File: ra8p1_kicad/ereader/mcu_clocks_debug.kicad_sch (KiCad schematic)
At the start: 20 parts, among them U1 R7KA8P1KFLCAC#UC0

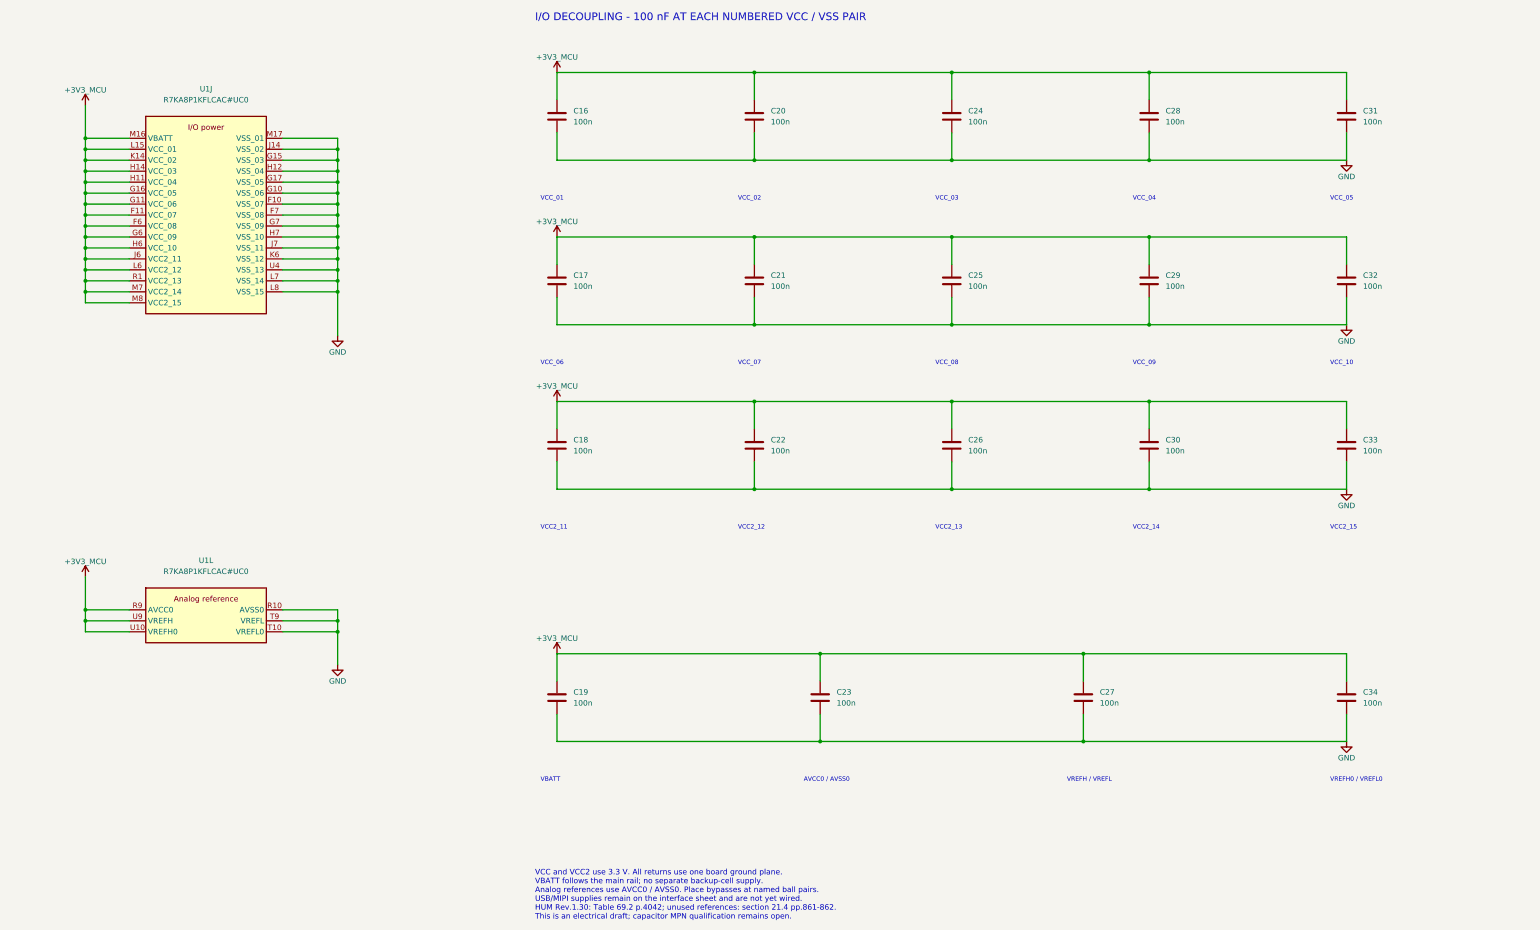
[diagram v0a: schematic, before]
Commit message: feat(hardware): add RA8P1 boot debug draft and refine schematic presentation
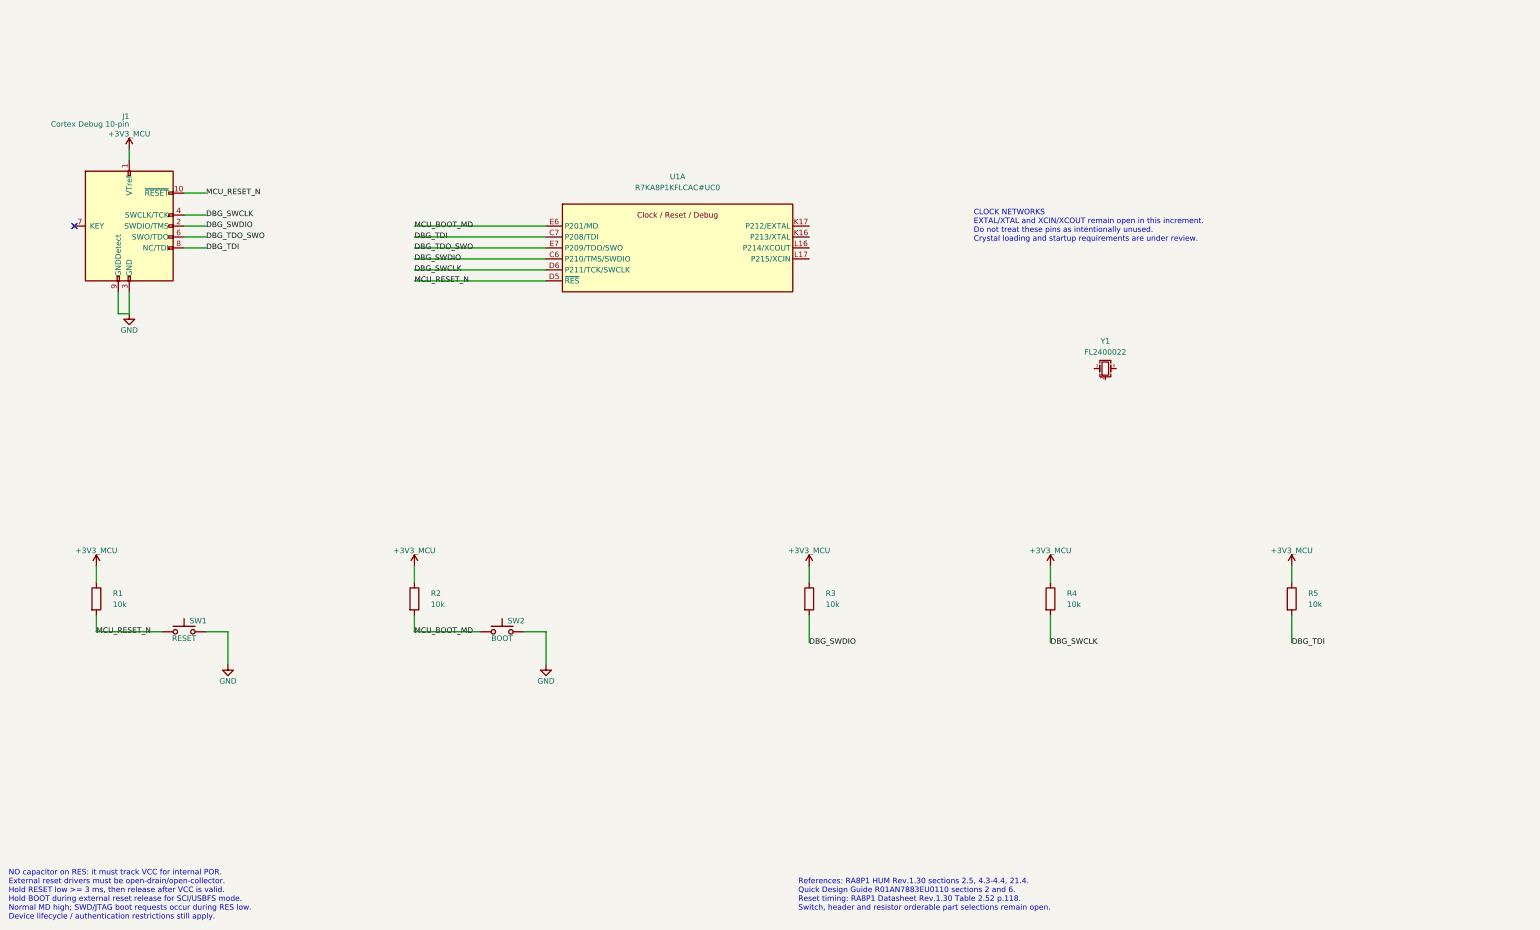
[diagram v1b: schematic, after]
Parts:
- removed C16, C17, C18, C19, C20, C21, C22, C23, C24, C25, C26, C27, C28, C29, C30, C31, C32, C33, C34: 100n, symbol Device:C
- removed U1: R7KA8P1KFLCAC#UC0, Processors:BGA289C65P17X17_1200X1200X138, symbol Processors:R7KA8P1KFLCAC#UC0
- added J1: Cortex Debug 10-pin, symbol Connectors:Cortex_Debug_10_Key
- added R1, R2, R3, R4, R5: 10k, symbol Device:R
- added SW1: RESET, symbol Switch:SW_Push
- added SW2: BOOT, symbol Switch:SW_Push
- added U1: R7KA8P1KFLCAC#UC0, Processors:BGA289C65P17X17_1200X1200X138, symbol Processors:R7KA8P1KFLCAC#UC0
- added Y1: FL2400022, Timing:FL2400022, symbol Device:Crystal_GND24_Small
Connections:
- net +3V3_MCU: now also J1.1 (VTref), R1.1, R2.1, R3.1, R4.1, R5.1
- net GND: now also J1.3 (GND), J1.5 (GND), J1.9 (GNDDetect), SW1.2, SW2.2
- new net: Y1.2 (G), Y1.4 (G)
- new net DBG_SWCLK: J1.4 (SWCLK/TCK), R4.2, U1.D6 (P211/TCK/SWCLK)
- new net DBG_SWDIO: J1.2 (SWDIO/TMS), R3.2, U1.C6 (P210/TMS/SWDIO)
- new net DBG_TDI: J1.8 (NC/TDI), R5.2, U1.C7 (P208/TDI)
- new net DBG_TDO_SWO: J1.6 (SWO/TDO), U1.E7 (P209/TDO/SWO)
- new net MCU_BOOT_MD: R2.2, SW2.1, U1.E6 (P201/MD)
- new net MCU_RESET_N: J1.10 (~{RESET}), R1.2, SW1.1, U1.D5 (~{RES})
- no-connect marks 0 -> 1
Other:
- note added: "CLOCK NETWORKS EXTAL/XTAL and XCIN/XCOUT remain open in this increment. Do not treat these pins as intentionally unused. Crystal loading and startup requirements are under review."
- note added: "NO capacitor on RES: it must track VCC for internal POR. External reset drivers must be open-drain/open-collector. Hold RESET low >= 3 ms, then release after VCC is valid. Hold BOOT during external reset release for SCI/USBFS mode. Normal MD high; SWD/JTAG boot requests occur during RES low. Device lifecycle / authentication restrictions still apply."
- note added: "References: RA8P1 HUM Rev.1.30 sections 2.5, 4.3-4.4, 21.4. Quick Design Guide R01AN7883EU0110 sections 2 and 6. Reset timing: RA8P1 Datasheet Rev.1.30 Table 2.52 p.118. Switch, header and resistor orderable part selections remain open."
- note removed: "AVCC0 / AVSS0"
- note removed: "I/O DECOUPLING - 100 nF AT EACH NUMBERED VCC / VSS PAIR"
- note removed: "VBATT"
- note removed: "VCC and VCC2 use 3.3 V. All returns use one board ground plane. VBATT follows the main rail; no separate backup-cell supply. Analog references use AVCC0 / AVSS0. Place bypasses at named ball pairs. USB/MIPI supplies remain on the interface sheet and are not yet wired. HUM Rev.1.30: Table 69.2 p.4042; unused references: section 21.4 pp.861-862. This is an electrical draft; capacitor MPN qualificat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"
- note removed: "VCC2_11"
- note removed: "VCC2_12"
- note removed: "VCC2_13"
- note removed: "VCC2_14"
- note removed: "VCC2_15"
- note removed: "VCC_01"
- note removed: "VCC_02"
- note removed: "VCC_03"
- note removed: "VCC_04"
- note removed: "VCC_05"
- note removed: "VCC_06"
- note removed: "VCC_07"
- note removed: "VCC_08"
- note removed: "VCC_09"
- note removed: "VCC_10"
- note removed: "VREFH / VREFL"
- note removed: "VREFH0 / VREFL0"
- company: RA8P1 e-reader -> (none)
- title: RA8P1 I/O and analog supplies -> RA8P1 clocks, reset and debug

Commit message: feat(hardware): track schematic BOM and DigiKey sourcing risks
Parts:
- J1: Procurement_Status (none) -> TBD - qualify keyed Cortex 10-pin connector and exact MPN
- R1, R2, R3, R4, R5: Procurement_Status (none) -> TBD - source common 10k 1% resistor with suitable ratings
- SW1, SW2: Procurement_Status (none) -> TBD - source normally-open momentary switch; mechanical cho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
- U1: DigiKey_Part_Number (none) -> 559-R7KA8P1KFLCAC#UC0-ND; DigiKey_URL (none) -> https://www.digikey.com/en/products/detail/renesas-electron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; Procurement_Status (none) -> HOLD - DigiKey discontinued; qualify orderable RA8P1 suffix; Sourcing_Snapshot (none) -> 2026-09-05 indexed: stock 1; USD 29.47; no backorders. Dist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
- Y1: Procurement_Status (none) -> HOLD - oscillator matching and exact MPN sourcing pending
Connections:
- net GND: now also Y1.2 (G), Y1.4 (G)

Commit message: feat(hardware): add Mouser sourcing and qualify MCU pull-up resistors
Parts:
- R1, R2, R3, R4, R5: DigiKey_Part_Number (none) -> 311-10.0KHRCT-ND; DigiKey_URL (none) -> https://www.digikey.com/en/products/detail/yageo/RC0603FR-0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; Manufacturer_Name (none) -> YAGEO; Manufacturer_Part_Number (none) -> RC0603FR-0710KL; Procurement_Status TBD - source common 10k 1% resistor with suitable ratings -> Selected - electrical ratings and sourcing checked; footpri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; Selection_Basis (none) -> 10k 1%, 100mW at 70C, 0603; 3.6V/9.9k=0.364mA and 1.31mW wo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; Sourcing_Snapshot (none) -> 2026-09-05 indexed: stock 2922248; Active; USD CT 1:0.10 / 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
- U1: Mouser Part Number (none) -> 968-R7KA8P1KFLCACUC0; Mouser Price/Stock (none) -> 2026-09-05 browser: 317 in stock; USD 1:29.47 / 10:23.82 / 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; Mouser_URL (none) -> https://www.mouser.com/en/ProductDetail/Renesas-Electronics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; Procurement_Status HOLD - DigiKey discontinued; qualify orderable RA8P1 suffix -> Retain exact UC0 - Mouser stock verified; circuit qualifica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

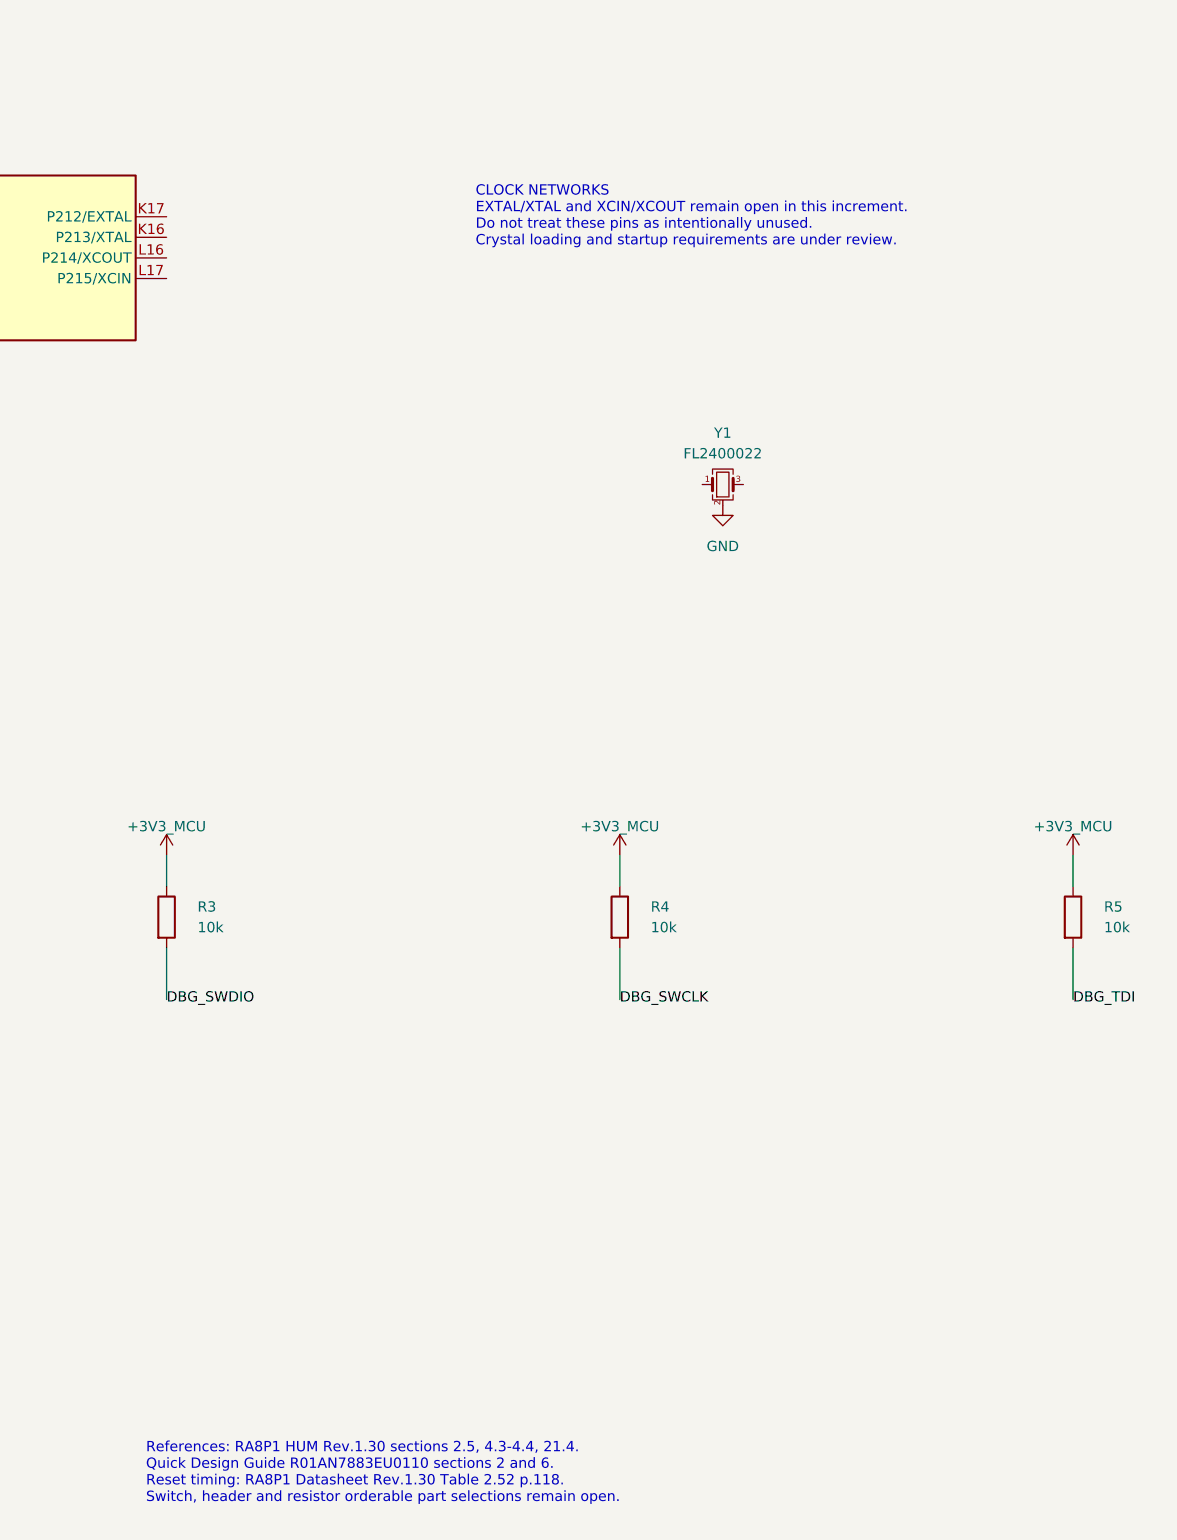
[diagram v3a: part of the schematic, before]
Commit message: feat(hardware): wire main oscillator with traceable load calculations
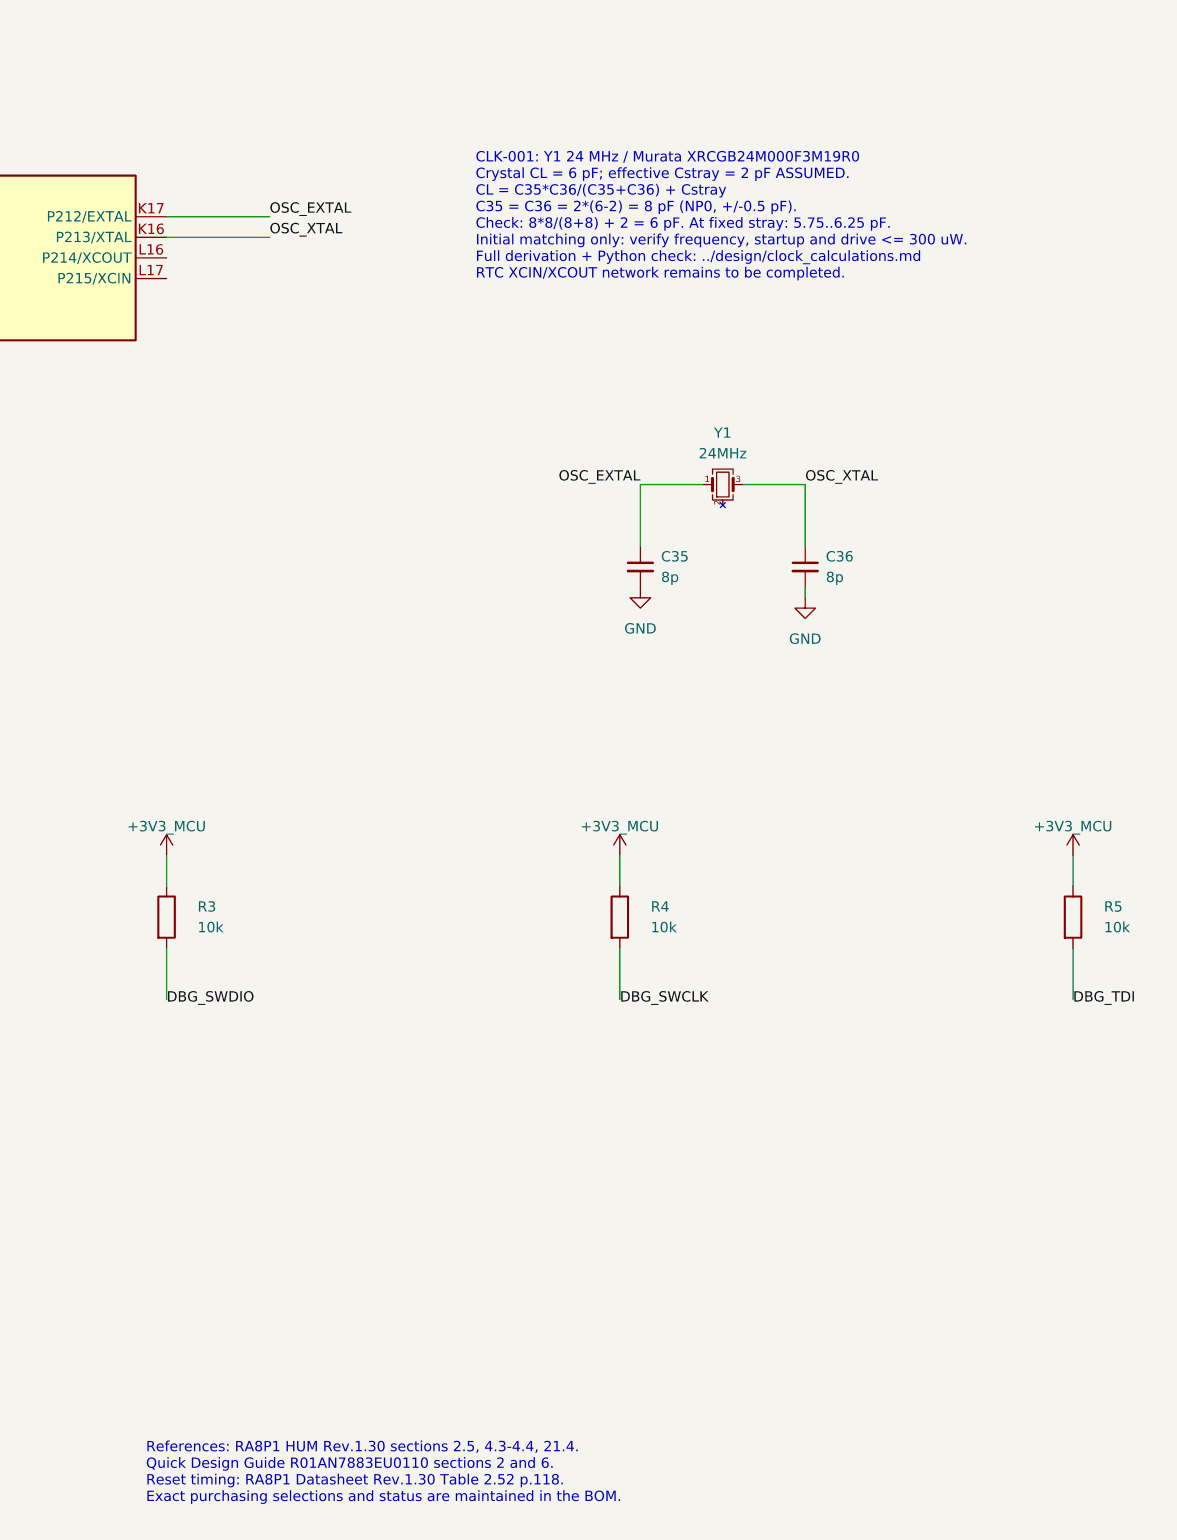
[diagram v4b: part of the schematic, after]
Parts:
- added C35, C36: 8p, symbol Device:C_Small
- Y1: value FL2400022 -> 24MHz; footprint Timing:FL2400022 -> (none); symbol Device:Crystal_GND24_Small -> Timing:XRCGB24M000F3M19R0; DigiKey_Part_Number (none) -> 490-18296-1-ND; DigiKey_URL (none) -> https://www.digikey.com/en/products/detail/murata-electroni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; Height 0.78 -> 0.70; Manufacturer_Name Diodes Incorporated -> Murata Electronics; Manufacturer_Part_Number FL2400022 -> XRCGB24M000F3M19R0; Mouser Part Number 729-FL2400022 -> (none); Mouser Price/Stock https://www.mouser.co.uk/ProductDetail/Diodes-Incorporated/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 -> (none); Procurement_Status HOLD - oscillator matching and exact MPN sourcing pending -> Selected for schematic - board oscillator matching required; Selection_Basis (none) -> Murata JGC49-3003B: 24MHz, CL6pF, ESR<=100 ohm, drive<=300u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; Sourcing_Snapshot (none) -> 2026-09-05 indexed: stock 13578; Active; USD CT 1:0.32 / 10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
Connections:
- net GND: now also C35.2, C36.2; no longer Y1.2 (G), Y1.4 (G)
- net OSC_XTAL: now reaches U1.K16 (P213/XTAL)
- net OSC_XTAL: now also Y1.3, C36.1
- net OSC_EXTAL: now reaches U1.K17 (P212/EXTAL)
- net OSC_EXTAL: now also Y1.1, C35.1
- new net: Y1.2 (NC), Y1.4 (NC)
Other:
- note added: "CLK-001: Y1 24 MHz / Murata XRCGB24M000F3M19R0 Crystal CL = 6 pF; effective Cstray = 2 pF ASSUMED. CL = C35*C36/(C35+C36) + Cstray C35 = C36 = 2*(6-2) = 8 pF (NP0, +/-0.5 pF). Check: 8*8/(8+8) + 2 = 6 pF. At fixed stray: 5.75..6.25 pF. Initial matching only: verify frequency, startup and drive <= 300 uW. Full derivation + Python check: ../design/clock_calculations.md RTC XCIN/XCOUT network remain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"
- note added: "References: RA8P1 HUM Rev.1.30 sections 2.5, 4.3-4.4, 21.4. Quick Design Guide R01AN7883EU0110 sections 2 and 6. Reset timing: RA8P1 Datasheet Rev.1.30 Table 2.52 p.118. Exact purchasing selections and status are maintained in the BOM."
- note removed: "CLOCK NETWORKS EXTAL/XTAL and XCIN/XCOUT remain open in this increment. Do not treat these pins as intentionally unused. Crystal loading and startup requirements are under review."
- note removed: "References: RA8P1 HUM Rev.1.30 sections 2.5, 4.3-4.4, 21.4. Quick Design Guide R01AN7883EU0110 sections 2 and 6. Reset timing: RA8P1 Datasheet Rev.1.30 Table 2.52 p.118. Switch, header and resistor orderable part selections remain open."
